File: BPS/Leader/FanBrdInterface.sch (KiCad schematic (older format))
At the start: 14 parts, among them J13 FanBrdConn, U14 SI8261ABC-IS, U15 SI8261ABC-IS, U16 SI8261ABC-IS, U17 SI8261ABC-IS

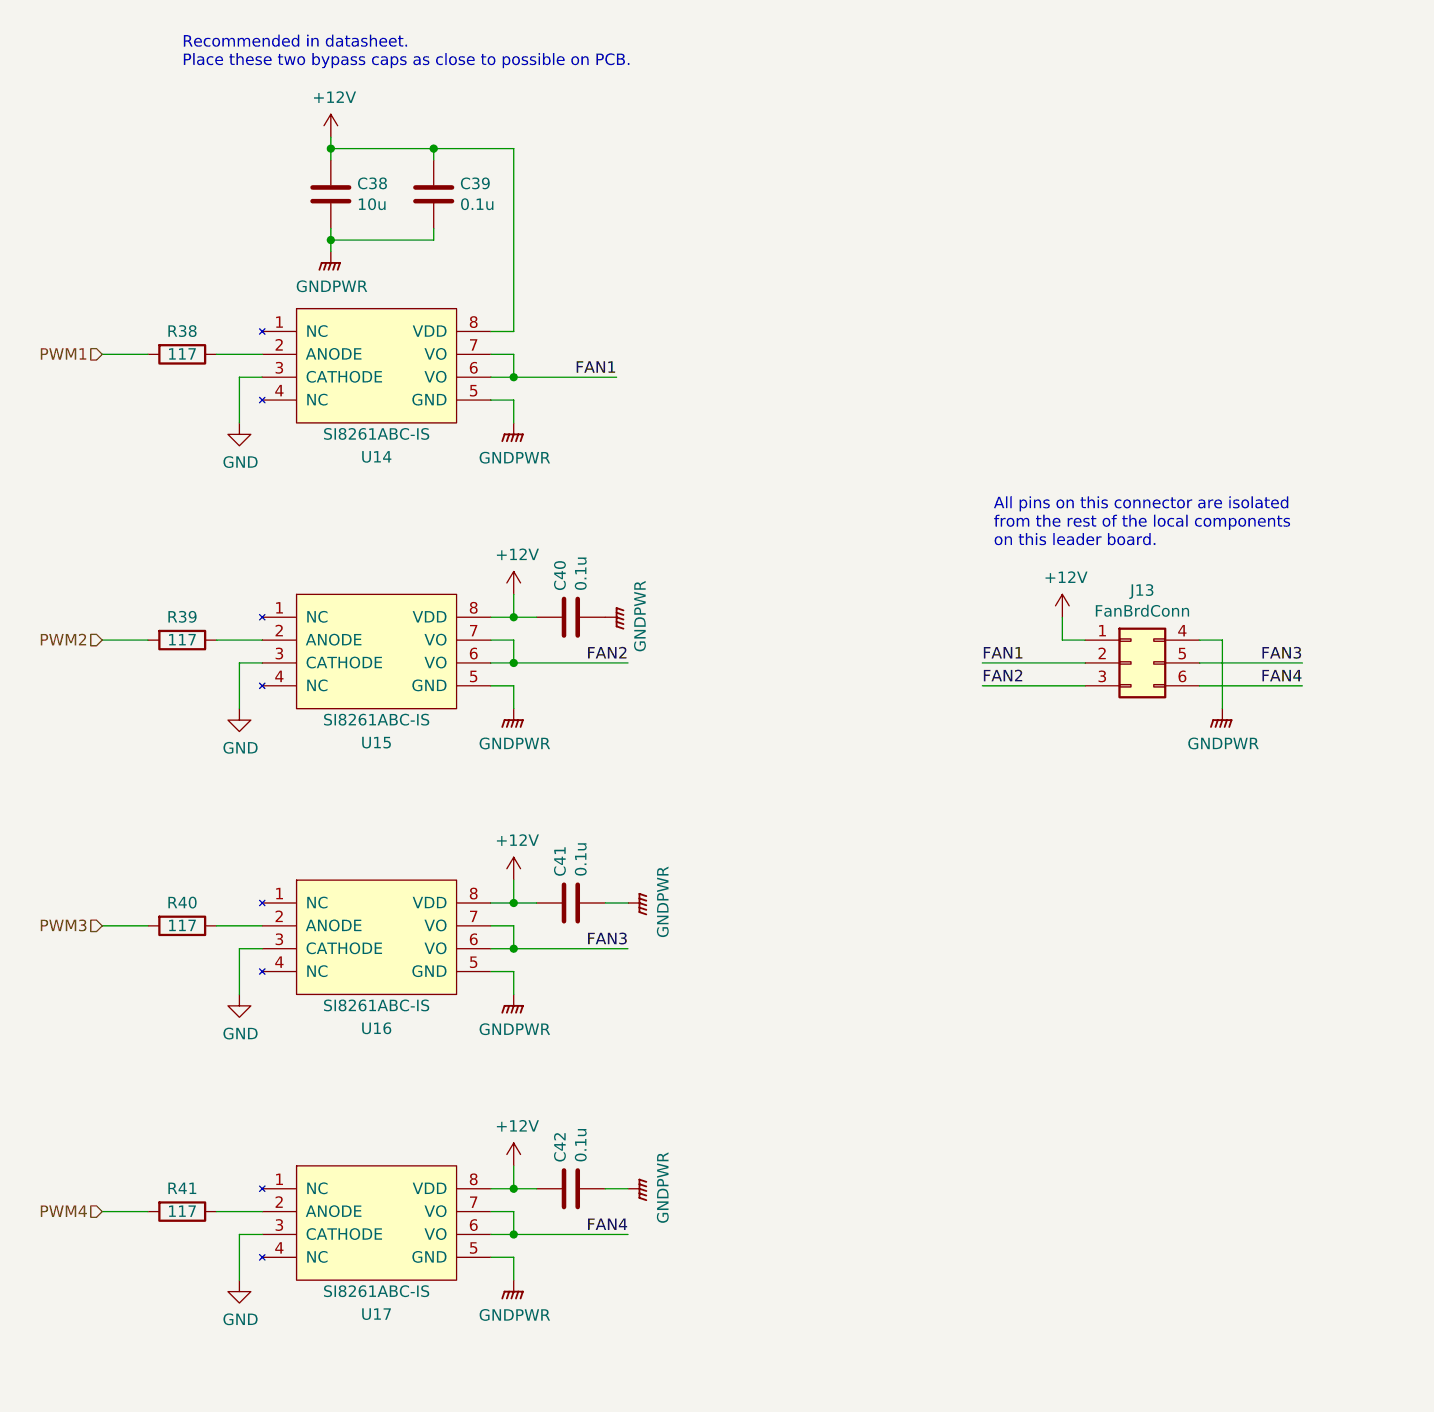
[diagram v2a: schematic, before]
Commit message: Finished leader board
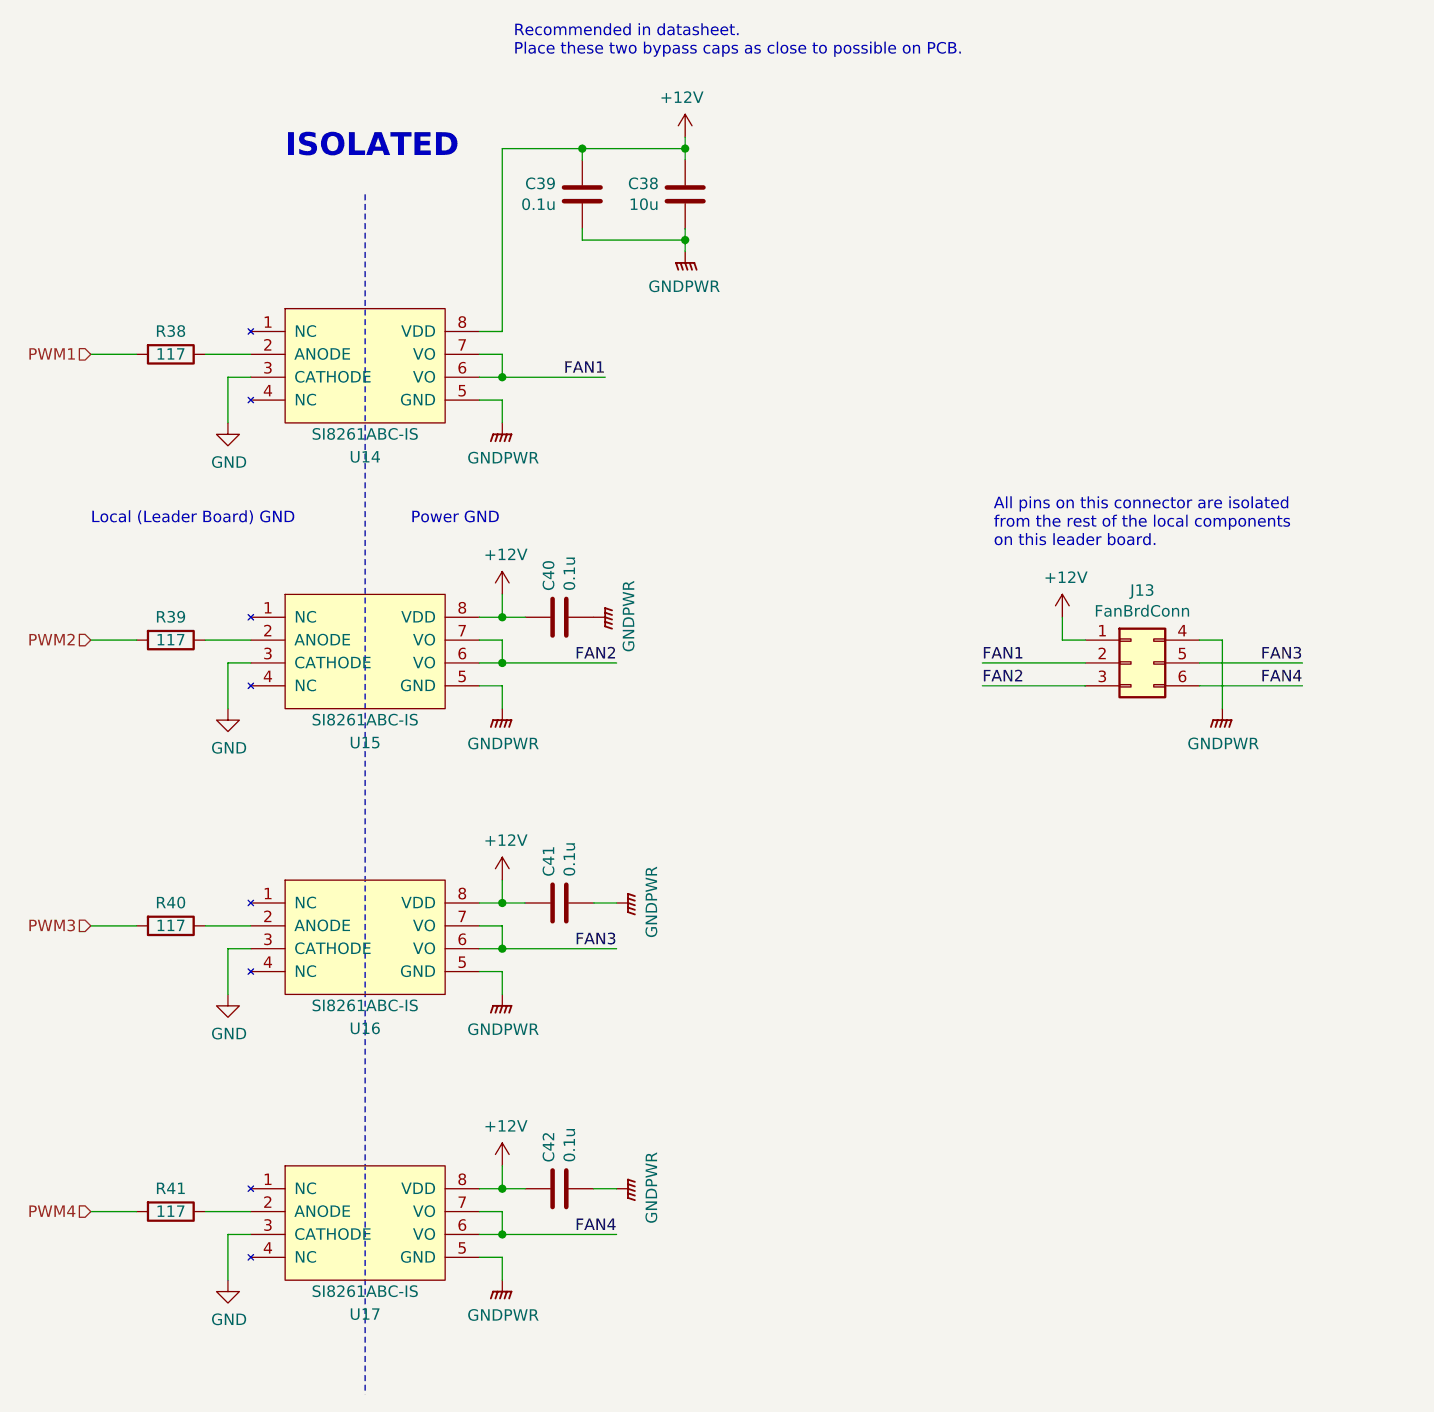
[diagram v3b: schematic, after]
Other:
- note added: "ISOLATED"
- note added: "Local (Leader Board) GND"
- note added: "Power GND"
- moved on the sheet: C38, C39, C40, C41, C42, R38, R39, R40, R41, U14, U15, U16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

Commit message: Simplifies dc-dc converter schematics
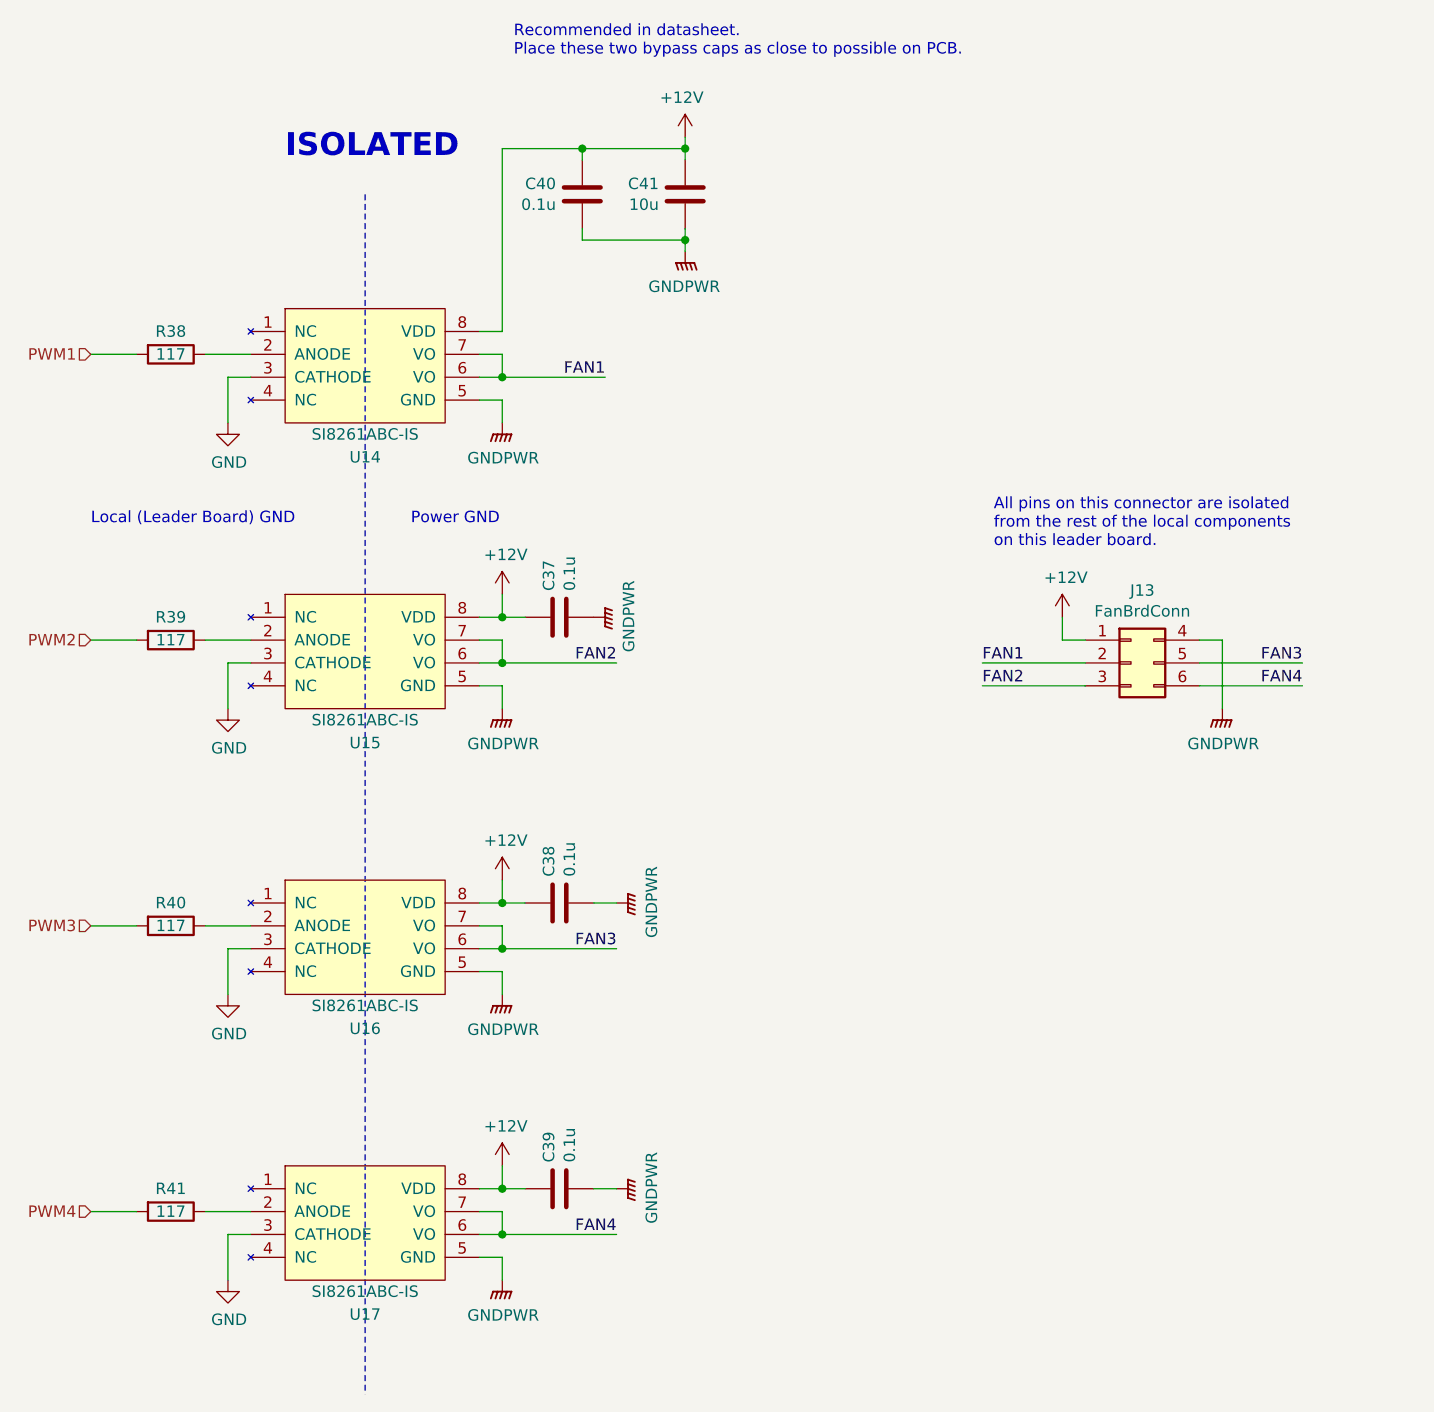
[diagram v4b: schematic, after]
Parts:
- renumbered C40 to C37, C41 to C38, C42 to C39, C39 to C40, C38 to C41
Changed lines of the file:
@@
 P 5650 1750
 AR Path="/5C38C674/5F130099" Ref="#PWR?"  Part="1"
-AR Path="/5F145F02/5F130099" Ref="#PWR085"  Part="1"
-F 0 "#PWR085" H 5650 1600 50  0001 C CNN
+AR Path="/5F145F02/5F130099" Ref="#PWR094"  Part="1"
+F 0 "#PWR094" H 5650 1600 50  0001 C CNN
 F 1 "+12V" H 5665 1923 50  0000 C CNN
 F 2 "" H 5650 1750 50  0001 C CNN
@@
 P 5650 2000
 AR Path="/5C38C674/5F13009F" Ref="C?"  Part="1"
-AR Path="/5F145F02/5F13009F" Ref="C38"  Part="1"
-F 0 "C38" H 5765 2046 50  0000 L CNN
+AR Path="/5F145F02/5F13009F" Ref="C41"  Part="1"
+F 0 "C41" H 5765 2046 50  0000 L CNN
 F 1 "10u" H 5765 1955 50  0000 L CNN
 F 2 "Capacitor_SMD:C_0805_2012Metric" H 5688 1850 50  0001 C CNN
@@
 P 5200 2000
 AR Path="/5C38C674/5F1300A5" Ref="C?"  Part="1"
-AR Path="/5F145F02/5F1300A5" Ref="C39"  Part="1"
-F 0 "C39" H 5315 2046 50  0000 L CNN
+AR Path="/5F145F02/5F1300A5" Ref="C40"  Part="1"
+F 0 "C40" H 5315 2046 50  0000 L CNN
 F 1 "0.1u" H 5315 1955 50  0000 L CNN
 F 2 "Capacitor_SMD:C_0805_2012Metric" H 5238 1850 50  0001 C CNN
@@
 P 5650 2250
 AR Path="/5C38C674/5F1300F5" Ref="#PWR?"  Part="1"
-AR Path="/5F145F02/5F1300F5" Ref="#PWR086"  Part="1"
-F 0 "#PWR086" H 5650 2050 50  0001 C CNN
+AR Path="/5F145F02/5F1300F5" Ref="#PWR095"  Part="1"
+F 0 "#PWR095" H 5650 2050 50  0001 C CNN
 F 1 "GNDPWR" H 5654 2096 50  0000 C CNN
 F 2 "" H 5650 2200 50  0001 C CNN
@@
 P 4850 3000
 AR Path="/5C38C674/5F1300FB" Ref="#PWR?"  Part="1"
-AR Path="/5F145F02/5F1300FB" Ref="#PWR087"  Part="1"
-F 0 "#PWR087" H 4850 2800 50  0001 C CNN
+AR Path="/5F145F02/5F1300FB" Ref="#PWR084"  Part="1"
+F 0 "#PWR084" H 4850 2800 50  0001 C CNN
 F 1 "GNDPWR" H 4854 2846 50  0000 C CNN
 F 2 "" H 4850 2950 50  0001 C CNN
@@
 	4850 2700 4850 2800
 $Comp
-L power:GND #PWR081
+L power:GND #PWR080
 U 1 1 5F1328D9
 P 3650 3000
-F 0 "#PWR081" H 3650 2750 50  0001 C CNN
+F 0 "#PWR080" H 3650 2750 50  0001 C CNN
 F 1 "GND" H 3655 2827 50  0000 C CNN
 F 2 "" H 3650 3000 50  0001 C CNN
@@
 P 4850 3750
 AR Path="/5C38C674/5F1531CC" Ref="#PWR?"  Part="1"
-AR Path="/5F145F02/5F1531CC" Ref="#PWR088"  Part="1"
-F 0 "#PWR088" H 4850 3600 50  0001 C CNN
+AR Path="/5F145F02/5F1531CC" Ref="#PWR085"  Part="1"
+F 0 "#PWR085" H 4850 3600 50  0001 C CNN
 F 1 "+12V" H 4865 3923 50  0000 C CNN
 F 2 "" H 4850 3750 50  0001 C CNN
@@
 P 4850 4250
 AR Path="/5C38C674/5F1531F5" Ref="#PWR?"  Part="1"
-AR Path="/5F145F02/5F1531F5" Ref="#PWR089"  Part="1"
-F 0 "#PWR089" H 4850 4050 50  0001 C CNN
+AR Path="/5F145F02/5F1531F5" Ref="#PWR086"  Part="1"
+F 0 "#PWR086" H 4850 4050 50  0001 C CNN
 F 1 "GNDPWR" H 4854 4096 50  0000 C CNN
 F 2 "" H 4850 4200 50  0001 C CNN
@@
 	4850 3950 4850 4050
 $Comp
-L power:GND #PWR082
+L power:GND #PWR081
 U 1 1 5F1531FD
 P 3650 4250
-F 0 "#PWR082" H 3650 4000 50  0001 C CNN
+F 0 "#PWR081" H 3650 4000 50  0001 C CNN
 F 1 "GND" H 3655 4077 50  0000 C CNN
 F 2 "" H 3650 4250 50  0001 C CNN
@@
 P 4850 5000
 AR Path="/5C38C674/5F155440" Ref="#PWR?"  Part="1"
-AR Path="/5F145F02/5F155440" Ref="#PWR090"  Part="1"
-F 0 "#PWR090" H 4850 4850 50  0001 C CNN
+AR Path="/5F145F02/5F155440" Ref="#PWR087"  Part="1"
+F 0 "#PWR087" H 4850 4850 50  0001 C CNN
 F 1 "+12V" H 4865 5173 50  0000 C CNN
 F 2 "" H 4850 5000 50  0001 C CNN
@@
 P 4850 5500
 AR Path="/5C38C674/5F155469" Ref="#PWR?"  Part="1"
-AR Path="/5F145F02/5F155469" Ref="#PWR091"  Part="1"
-F 0 "#PWR091" H 4850 5300 50  0001 C CNN
+AR Path="/5F145F02/5F155469" Ref="#PWR088"  Part="1"
+F 0 "#PWR088" H 4850 5300 50  0001 C CNN
 F 1 "GNDPWR" H 4854 5346 50  0000 C CNN
 F 2 "" H 4850 5450 50  0001 C CNN
@@
 	4850 5200 4850 5300
 $Comp
-L power:GND #PWR083
+L power:GND #PWR082
 U 1 1 5F155471
 P 3650 5500
-F 0 "#PWR083" H 3650 5250 50  0001 C CNN
+F 0 "#PWR082" H 3650 5250 50  0001 C CNN
 F 1 "GND" H 3655 5327 50  0000 C CNN
 F 2 "" H 3650 5500 50  0001 C CNN
@@
 FAN3
 $Comp
-L power:+12V #PWR097
+L power:+12V #PWR096
 U 1 1 5F157D4C
 P 7300 3850
-F 0 "#PWR097" H 7300 3700 50  0001 C CNN
+F 0 "#PWR096" H 7300 3700 50  0001 C CNN
 F 1 "+12V" H 7315 4023 50  0000 C CNN
 F 2 "" H 7300 3850 50  0001 C CNN
@@
 P 8000 4250
 AR Path="/5C38C674/5F15A290" Ref="#PWR?"  Part="1"
-AR Path="/5F145F02/5F15A290" Ref="#PWR098"  Part="1"
-F 0 "#PWR098" H 8000 4050 50  0001 C CNN
+AR Path="/5F145F02/5F15A290" Ref="#PWR097"  Part="1"
+F 0 "#PWR097" H 8000 4050 50  0001 C CNN
 F 1 "GNDPWR" H 8004 4096 50  0000 C CNN
 F 2 "" H 8000 4200 50  0001 C CNN
@@
 P 4850 6250
 AR Path="/5C38C674/5F1644DE" Ref="#PWR?"  Part="1"
-AR Path="/5F145F02/5F1644DE" Ref="#PWR092"  Part="1"
-F 0 "#PWR092" H 4850 6100 50  0001 C CNN
+AR Path="/5F145F02/5F1644DE" Ref="#PWR089"  Part="1"
+F 0 "#PWR089" H 4850 6100 50  0001 C CNN
 F 1 "+12V" H 4865 6423 50  0000 C CNN
 F 2 "" H 4850 6250 50  0001 C CNN
@@
 P 4850 6750
 AR Path="/5C38C674/5F164507" Ref="#PWR?"  Part="1"
-AR Path="/5F145F02/5F164507" Ref="#PWR093"  Part="1"
-F 0 "#PWR093" H 4850 6550 50  0001 C CNN
+AR Path="/5F145F02/5F164507" Ref="#PWR090"  Part="1"
+F 0 "#PWR090" H 4850 6550 50  0001 C CNN
 F 1 "GNDPWR" H 4854 6596 50  0000 C CNN
 F 2 "" H 4850 6700 50  0001 C CNN
@@
 	4850 6450 4850 6550
 $Comp
-L power:GND #PWR084
+L power:GND #PWR083
 U 1 1 5F16450F
 P 3650 6750
-F 0 "#PWR084" H 3650 6500 50  0001 C CNN
+F 0 "#PWR083" H 3650 6500 50  0001 C CNN
 F 1 "GND" H 3655 6577 50  0000 C CNN
 F 2 "" H 3650 6750 50  0001 C CNN
@@
 P 5100 3850
 AR Path="/5C38C674/5F1CC902" Ref="C?"  Part="1"
-AR Path="/5F145F02/5F1CC902" Ref="C40"  Part="1"
-F 0 "C40" H 5215 3896 50  0000 L CNN
+AR Path="/5F145F02/5F1CC902" Ref="C37"  Part="1"
+F 0 "C37" H 5215 3896 50  0000 L CNN
 F 1 "0.1u" H 5215 3805 50  0000 L CNN
 F 2 "Capacitor_SMD:C_0805_2012Metric" H 5138 3700 50  0001 C CNN
@@
 P 5100 5100
 AR Path="/5C38C674/5F1CE8B4" Ref="C?"  Part="1"
-AR Path="/5F145F02/5F1CE8B4" Ref="C41"  Part="1"
-F 0 "C41" H 5215 5146 50  0000 L CNN
+AR Path="/5F145F02/5F1CE8B4" Ref="C38"  Part="1"
+F 0 "C38" H 5215 5146 50  0000 L CNN
 F 1 "0.1u" H 5215 5055 50  0000 L CNN
 F 2 "Capacitor_SMD:C_0805_2012Metric" H 5138 4950 50  0001 C CNN
@@
 P 5100 6350
 AR Path="/5C38C674/5F1D0348" Ref="C?"  Part="1"
-AR Path="/5F145F02/5F1D0348" Ref="C42"  Part="1"
-F 0 "C42" H 5215 6396 50  0000 L CNN
+AR Path="/5F145F02/5F1D0348" Ref="C39"  Part="1"
+F 0 "C39" H 5215 6396 50  0000 L CNN
 F 1 "0.1u" H 5215 6305 50  0000 L CNN
 F 2 "Capacitor_SMD:C_0805_2012Metric" H 5138 6200 50  0001 C CNN
@@
 P 5350 6350
 AR Path="/5C38C674/5F1D20B3" Ref="#PWR?"  Part="1"
-AR Path="/5F145F02/5F1D20B3" Ref="#PWR096"  Part="1"
-F 0 "#PWR096" H 5350 6150 50  0001 C CNN
+AR Path="/5F145F02/5F1D20B3" Ref="#PWR093"  Part="1"
+F 0 "#PWR093" H 5350 6150 50  0001 C CNN
 F 1 "GNDPWR" H 5354 6196 50  0000 C CNN
 F 2 "" H 5350 6300 50  0001 C CNN
@@
 P 5350 5100
 AR Path="/5C38C674/5F1D596F" Ref="#PWR?"  Part="1"
-AR Path="/5F145F02/5F1D596F" Ref="#PWR095"  Part="1"
-F 0 "#PWR095" H 5350 4900 50  0001 C CNN
+AR Path="/5F145F02/5F1D596F" Ref="#PWR092"  Part="1"
+F 0 "#PWR092" H 5350 4900 50  0001 C CNN
 F 1 "GNDPWR" H 5354 4946 50  0000 C CNN
 F 2 "" H 5350 5050 50  0001 C CNN
@@
 P 5250 3850
 AR Path="/5C38C674/5F1DA30D" Ref="#PWR?"  Part="1"
-AR Path="/5F145F02/5F1DA30D" Ref="#PWR094"  Part="1"
-F 0 "#PWR094" H 5250 3650 50  0001 C CNN
+AR Path="/5F145F02/5F1DA30D" Ref="#PWR091"  Part="1"
+F 0 "#PWR091" H 5250 3650 50  0001 C CNN
 F 1 "GNDPWR" H 5254 3696 50  0000 C CNN
 F 2 "" H 5250 3800 50  0001 C CNN
